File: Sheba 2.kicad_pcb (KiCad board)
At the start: 2 copper layers, 85.7 x 54 mm, 67 parts, among them J1 Conn_01x06_Pin, J2 Jack-DC, J3 GPIO, J4 Conn_01x02_Pin, J5 Conn_01x03_Pin, J6 Conn_01x03_Pin, J7 Conn_01x03_Pin, J8 Conn_01x03_Pin, SW1 SW_SPDT, U1 AP62150Z6, U2 MIC5504-3.3YM5, U4 STM32H503CBTx

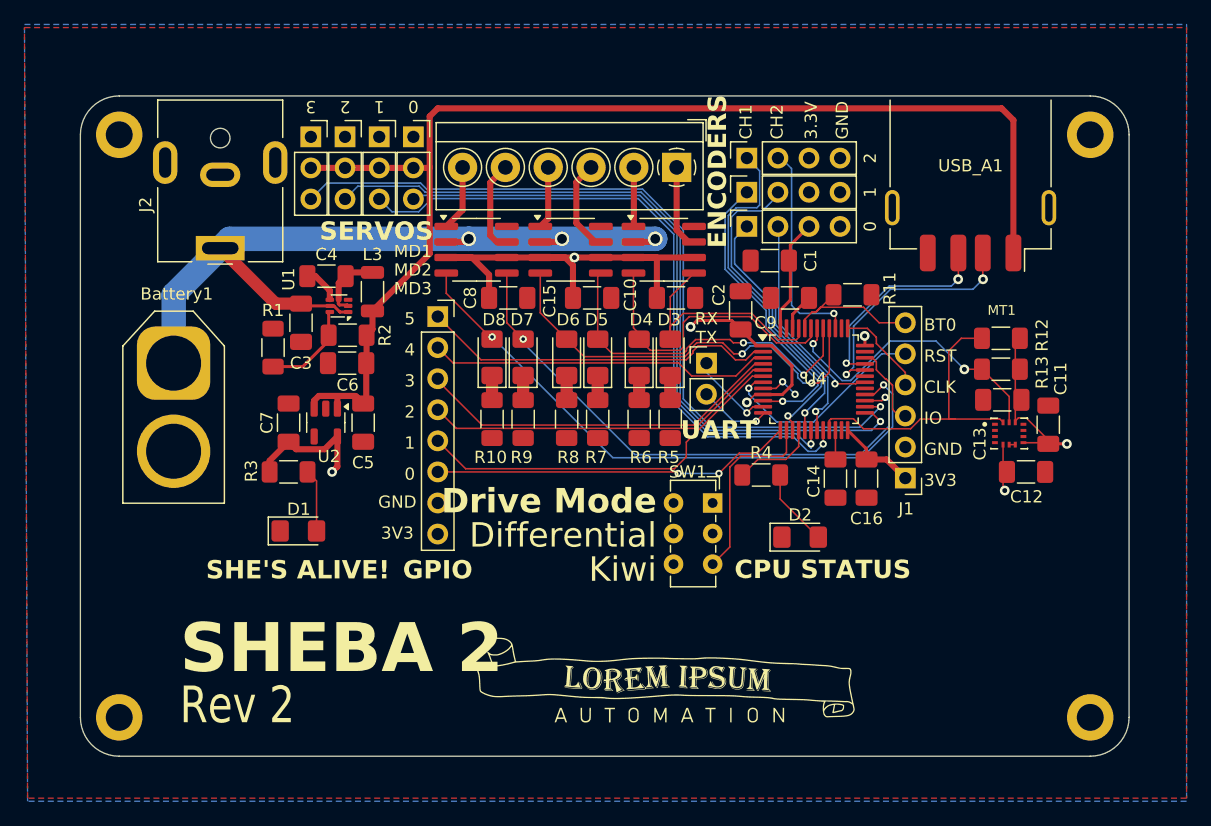
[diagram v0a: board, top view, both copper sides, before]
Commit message: Preparing to remove USB port and switch to STM32F072CBTx
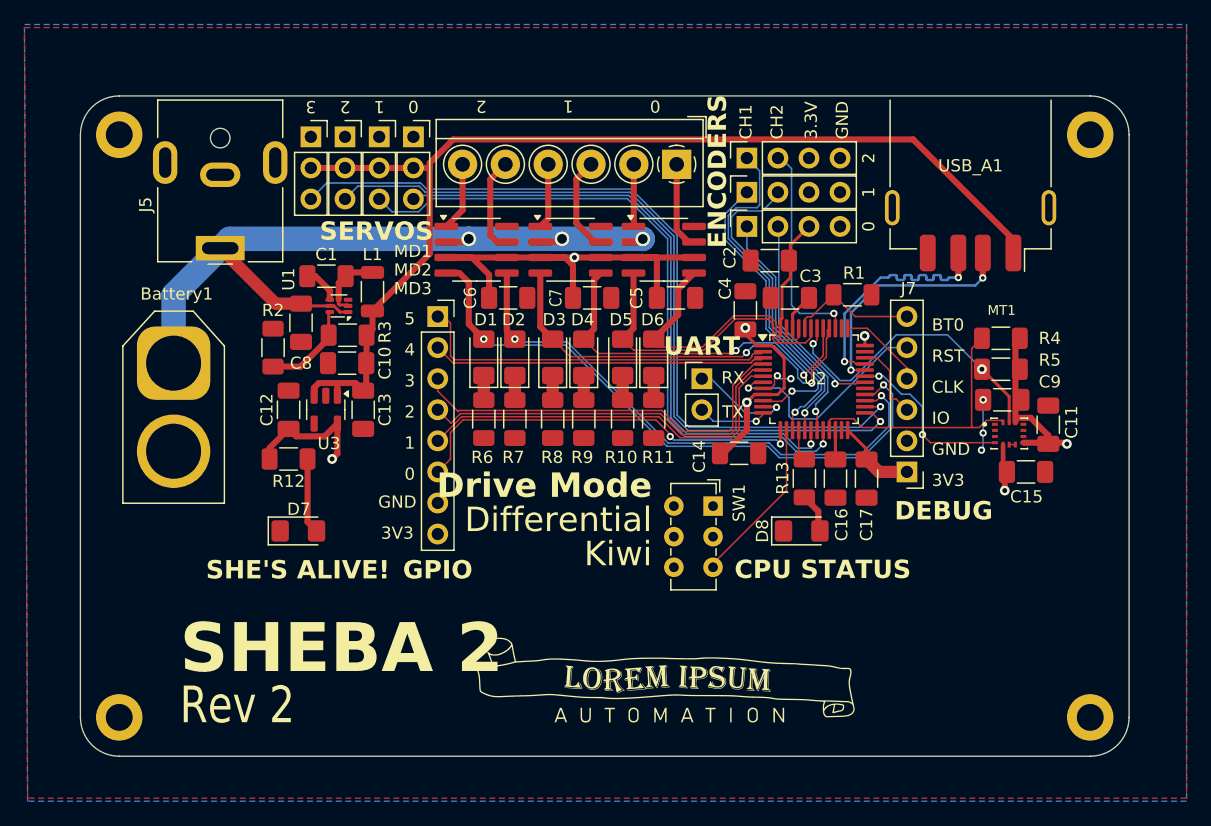
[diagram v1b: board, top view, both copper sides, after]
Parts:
- added C14: C1uF, Capacitor_SMD:C_1206_3216Metric_Pad1.33x1.80mm_HandSolder, F.Cu at (107.2, 59.2)
- moved R13 3.54 mm to (112.5, 61.2), turned to -90 degrees
- moved D5 1.35 mm to (97.7, 51.3)
- moved R10 1.35 mm to (97.7, 56.4)
- moved D6 1.35 mm to (100.2, 51.3)
- moved R11 1.35 mm to (100.2, 56.4)
- moved J8 1.33 mm to (104.1, 53.1)
- moved D3 1.14 mm to (91.9, 51.3)
- moved D4 1.14 mm to (94.5, 51.3)
- moved R8 1.14 mm to (91.9, 56.4)
- moved R9 1.14 mm to (94.5, 56.4)
- moved C12 1.05 mm to (70.4, 55.6)
- moved C13 1.05 mm to (76.5, 55.6)
- moved R12 1.05 mm to (70.4, 59.7)
- moved U3 1.05 mm to (73.4, 55.6)
- moved D1 0.68 mm to (86.3, 51.3)
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- renumbered C4 to C1, C6 to C10, C7 to C12, C5 to C13, C12 to C15, C14 to C16, C16 to C17, C1 to C2, C9 to C3, C2 to C4, C10 to C5, C8 to C6, C15 to C7, C3 to C8, C13 to C9, D8 to D1, D7 to D2, D6 to D3, D5 to D4, D4 to D5, D3 to D6, D1 to D7, D2 to D8, EP2 to EP1, EP3 to EP2, EP1 to EP3, J8 to J1, J7 to J2, J6 to J3, J5 to J4, J2 to J5, J3 to J6, J1 to J7, J4 to J8, L3 to L1, R11 to R1, R6 to R10, R5 to R11, R3 to R12, R4 to R13, R1 to R2, R2 to R3, R12 to R4, R13 to R5, R10 to R6, R9 to R7, R7 to R9, U4 to U2, U2 to U3
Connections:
- net /USB_DM renamed /USB_D-
- net /USB_DP renamed /USB_D+
- net Net-(MD1-OUT1) renamed /M3_OUT2
- net Net-(MD1-OUT2) renamed /M3_OUT1
- net Net-(MD2-OUT1) renamed /M2_OUT2
- net Net-(MD2-OUT2) renamed /M2_OUT1
- net Net-(MD3-OUT1) renamed /M1_OUT2
- net Net-(MD3-OUT2) renamed /M1_OUT1
- U2 pad 31: unconnected-(U4-PA10-Pad31) -> IMU_INT
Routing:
- net IMU_INT: track 0.00 -> 14.2 mm, vias 0 -> 2
- net +5V: track 102.1 -> 89.3 mm
- net BLINKY: track 6.92 -> 1.94 mm
- net GND: track 4.28 -> 7.76 mm, vias 2 -> 5
- net GPIO_0: track 29.7 -> 33.1 mm
- net Net-(D8-A): track 7.09 -> 3.72 mm
- net /USB_D+: track 17.3 -> 20.6 mm
- net GPIO_2: track 29.2 -> 32.3 mm
- net +BATT: track 65.6 -> 62.9 mm
- net M1_FWD: track 19.7 -> 22.3 mm
- net GPIO_3: track 30.3 -> 32.5 mm
- net I2C1_SDA: track 25.1 -> 23.3 mm
- net BOOT0: track 12.3 -> 10.6 mm
- net USART1_RX: track 6.97 -> 8.57 mm
- net +3V3: track 98.7 -> 97.2 mm
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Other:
- board text added: "DEBUG"

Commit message: Rev 2 ordered!
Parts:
- removed C16, C3: C2.2uF, Capacitor_SMD:C_1206_3216Metric_Pad1.33x1.80mm_HandSolder
- removed J1: Conn_01x03_Pin, Connector_PinSocket_2.54mm:PinSocket_1x03_P2.54mm_Vertical
- removed J5: Jack-DC, Connector_BarrelJack:BarrelJack_CUI_PJ-063AH_Horizontal
- removed J6: GPIO, Connector_PinSocket_2.54mm:PinSocket_1x08_P2.54mm_Vertical
- removed U2: STM32H503CBTx, Package_QFP:LQFP-48_7x7mm_P0.5mm
- removed USB_A1: USB_A, Connector_USB:USB_A_Receptacle_GCT_USB1046
- added J9: Conn_02x04_Top_Bottom, Connector_PinSocket_2.54mm:PinSocket_2x04_P2.54mm_Vertical, F.Cu at (127.1, 37.6)
- added P1: USB_C_Plug_USB2.0, Connector_USB:USB_C_Receptacle_GCT_USB4105-xx-A_16P_TopMnt_Horizontal, F.Cu at (135.3, 41.1)
- added R14: R10k, Resistor_SMD:R_1206_3216Metric_Pad1.30x1.75mm_HandSolder, F.Cu at (114.0, 48.1)
- added U4: STM32F072CBTx, Package_QFP:LQFP-48_7x7mm_P0.5mm, F.Cu at (109.1, 52.6)
- C5, C6, C7, R10, R11, R6, R7, R8, R9: moved to B.Cu
- R1: value R10k -> 5.11K; moved to B.Cu
- moved R1 18.8 mm to (134.4, 40.4), turned to -90 degrees
- moved J8 12.3 mm to (102.5, 65.3), turned to -90 degrees
- moved SW1 11.6 mm to (97.0, 55.1)
- moved R6 9.81 mm to (81.3, 48.0), turned to 90 degrees
- moved R7 9.81 mm to (83.8, 48.0), turned to 90 degrees
- moved Battery1 9.77 mm to (59.4, 42.2)
- moved R9 8.91 mm to (91.6, 48.0), turned to 90 degrees
- moved R8 8.91 mm to (89.0, 48.0), turned to 90 degrees
- moved R10 8.50 mm to (96.5, 48.0), turned to 90 degrees
- moved R11 8.50 mm to (99.1, 48.0), turned to 90 degrees
- moved D1 6.06 mm to (81.3, 48.0)
- moved D2 6.06 mm to (83.8, 48.0)
- moved C5 5.96 mm to (96.6, 43.9), turned to 180 degrees
- moved C17 5.62 mm to (115.1, 56.2), turned to -135 degrees
- moved C6 5.22 mm to (83.9, 43.7)
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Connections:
- net I2C1_SCL renamed I2C2_SCL
- net I2C1_SDA renamed I2C2_SDA
- C17 pad 1: GND -> +3V3
- C17 pad 2: +3V3 -> GND
- C2 pad 1: +3V3 -> GND
- C2 pad 2: GND -> +3V3
- J2 pad 3: SERVO_2 -> SERVO2
- J3 pad 3: SERVO_1 -> SERVO1
- J4 pad 3: SERVO_0 -> SERVO0
- J7 pad 3: SYS_SWDIO -> NRST
- J7 pad 4: SYS_SWCLK -> SYS_SWDIO
- J7 pad 5: NRST -> SYS_SWCLK
- J8 pad 1: USART1_RX -> USART3_RX
- J8 pad 2: USART1_TX -> USART3_TX
- R1 pad 1: BOOT0 -> GND
- R1 pad 2: GND -> Net-(P1-CC)
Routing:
- net SERVO_3: track 66.0 -> 0.00 mm, vias 1 -> 0
- net SERVO_2: track 62.4 -> 0.00 mm, vias 1 -> 0
- net SERVO_1: track 55.8 -> 0.00 mm, vias 1 -> 0
- net SERVO2: track 0.00 -> 52.4 mm, vias 0 -> 1
- net SERVO_0: track 50.9 -> 0.00 mm, vias 1 -> 0
- net SERVO1: track 0.00 -> 46.2 mm, vias 0 -> 1
- net SERVO0: track 0.00 -> 42.9 mm, vias 0 -> 1
- net GND: track 7.76 -> 43.1 mm
- net GPIO_0: track 33.1 -> 0.00 mm, vias 2 -> 0
- net GPIO_3: track 32.5 -> 0.00 mm
- net GPIO_1: track 32.3 -> 0.00 mm
- net GPIO_2: track 32.3 -> 0.00 mm
- net GPIO_5: track 29.5 -> 0.00 mm
- net USB_D-: track 0.00 -> 28.1 mm, vias 0 -> 2
- net USB_D+: track 0.00 -> 28.0 mm, vias 0 -> 2
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
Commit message: Post-rev 2 changes
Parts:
- moved R1 1.02 mm to (133.3, 40.4)
- moved EP1 0.12 mm to (104.9, 37.8)
- moved EP2 0.12 mm to (104.9, 35.1)
- moved EP3 0.12 mm to (104.9, 40.6)
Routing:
- net I2C2_SCL: track 32.6 -> 30.5 mm
- net I2C2_SDA: track 28.7 -> 26.7 mm
- net +3V3: track 73.7 -> 75.6 mm, vias 10 -> 11
- net GPIO4: track 24.0 -> 22.8 mm
- net GPIO3: track 24.5 -> 23.4 mm
- net Net-(P1-CC): track 2.92 -> 1.90 mm
- net M2_REV: track 21.6 -> 22.6 mm
- net SERVO2: track 52.4 -> 53.1 mm
- net TIM3_CH1: track 23.2 -> 22.5 mm
- net GND: track 43.1 -> 42.6 mm
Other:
- board text added: "5V"
- board text added: "PWM"
